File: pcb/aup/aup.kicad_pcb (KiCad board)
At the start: 6 copper layers, 100 x 80 mm, 95 parts, among them IC1 MT41K128M16JT-125_K, IC2 88E1512-A0-NNP2C000, J1 DF40C-100DS-0.4V_51, J2 DF40C-100DS-0.4V_51, J3 DF40C-100DS-0.4V_51, J4 DF40C-100DS-0.4V_51, Q1 AO3401A, Q2 AO3401A, U1 XC7A50T-FGG484, U11 FT2232HQ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

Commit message: First pass on lower rails
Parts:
- F1, Q1: moved to B.Cu
- moved Q1 110.4 mm to (122.5, 54.0), turned to 180 degrees
- moved F1 105.6 mm to (118.0, 56.2), turned to 90 degrees
- moved R24 97.0 mm to (127.1, 124.5), turned to -90 degrees
- moved L5 96.9 mm to (121.4, 121.8), turned to -90 degrees
- moved R25 96.3 mm to (128.7, 124.5), turned to 90 degrees
- moved U7 95.7 mm to (124.5, 120.7)
- moved C25 93.2 mm to (124.5, 118.6)
- moved R26 92.0 mm to (128.7, 121.0), turned to 90 degrees
- moved R27 89.2 mm to (127.1, 121.0), turned to -90 degrees
- moved R32 88.5 mm to (113.7, 124.5), turned to 90 degrees
- moved C32 84.7 mm to (122.7, 125.8)
- moved R33 83.5 mm to (113.7, 121.0), turned to 90 degrees
- moved C29 83.0 mm to (122.7, 124.2)
- moved C21 81.1 mm to (121.3, 116.6), turned to 180 degrees
- moved L7 80.6 mm to (106.4, 121.8), turned to -90 degrees
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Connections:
- net Net-(U4-FB) renamed /power_reg/FB_1V2
- net Net-(U7-FB) renamed /power_reg/FB_1V35
- net Net-(U9-FB) renamed /power_reg/FB_3V3
- R30 pad 2: Net-(U8-FB) -> /power_reg/FB_Vccint
- R31 pad 1: Net-(U8-FB) -> /power_reg/FB_Vccint
- U8 pad 6: Net-(U8-FB) -> /power_reg/FB_Vccint
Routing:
- net +3V3: track 0.00 -> 15.2 mm, vias 0 -> 9
- net +1V35: track 0.00 -> 15.2 mm, vias 0 -> 9
- net GND: track 10.4 -> 15.6 mm, vias 41 -> 61
- net /power_reg/PG_3V3: track 0.00 -> 3.64 mm, vias 0 -> 2
- net /power_reg/PG_1V35: track 0.00 -> 3.64 mm, vias 0 -> 2
- net /power_reg/FB_3V3: track 0.00 -> 3.41 mm
- net /power_reg/FB_1V35: track 0.00 -> 3.41 mm
- net Net-(U8-FB): track 3.41 -> 0.00 mm
- net /power_reg/FB_Vccint: track 3.41 -> 6.82 mm
- net +5V: track 16.3 -> 19.5 mm, vias 17 -> 23
- net /power_reg/SW_3V3: track 0.00 -> 2.30 mm
- net /power_reg/SW_1V35: track 0.00 -> 2.30 mm
- net Net-(R32-Pad2): track 0.00 -> 1.83 mm
- net Net-(R25-Pad2): track 0.00 -> 1.83 mm
- added copper zone on F.Cu, net +1V35
- added copper zone on F.Cu, net +3V3
- added copper zone on In2.Cu, net +5V
- added copper zone on In2.Cu, net +Vccint
- added copper zone on F.Cu, net /power_reg/SW_1V35
- added copper zone on F.Cu, net /power_reg/SW_3V3
- added copper zone on In1.Cu, net GND
- added copper zone on In4.Cu, net GND
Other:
- board text added: "1V35"
- board text added: "3V3"

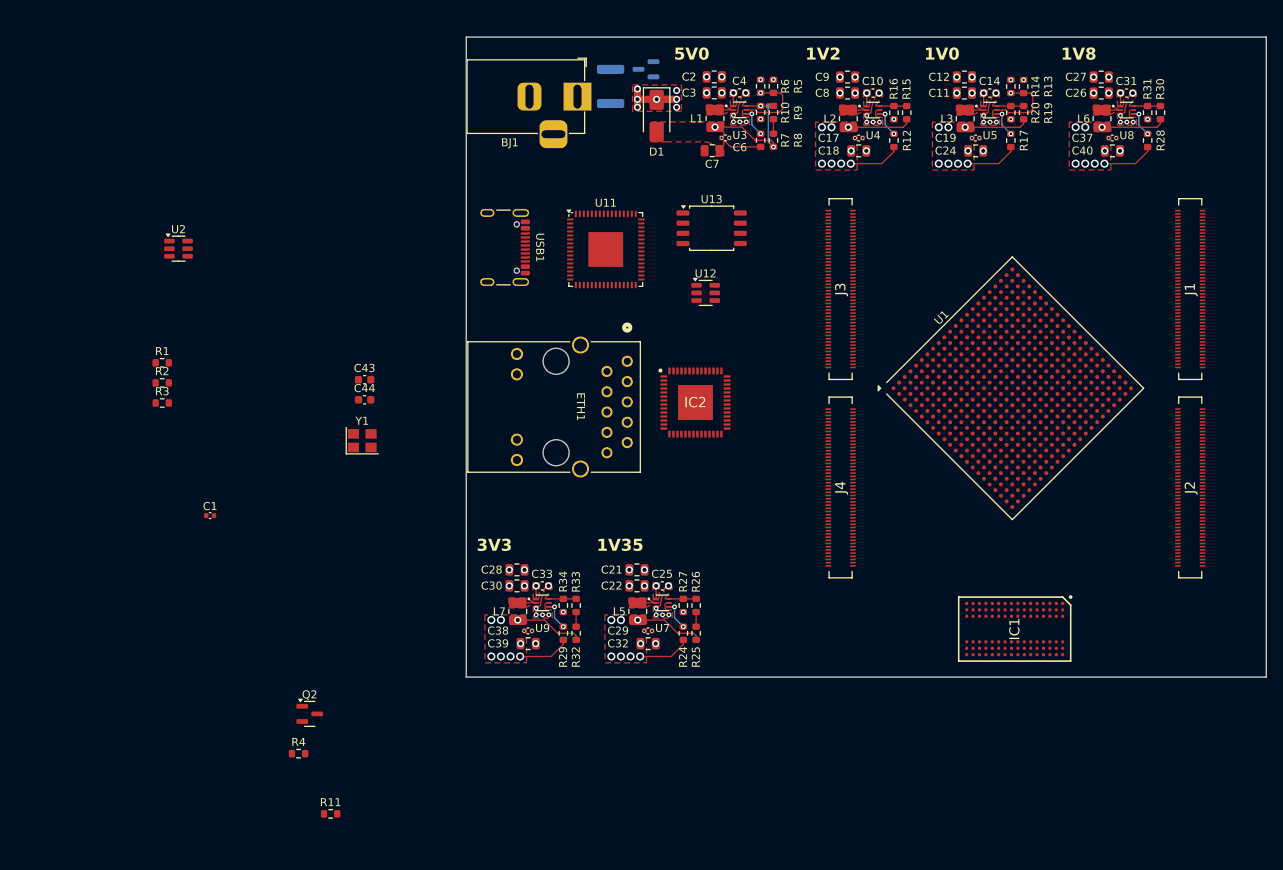
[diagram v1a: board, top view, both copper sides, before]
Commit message: Fix L1 footprint and add reg and ftdi models
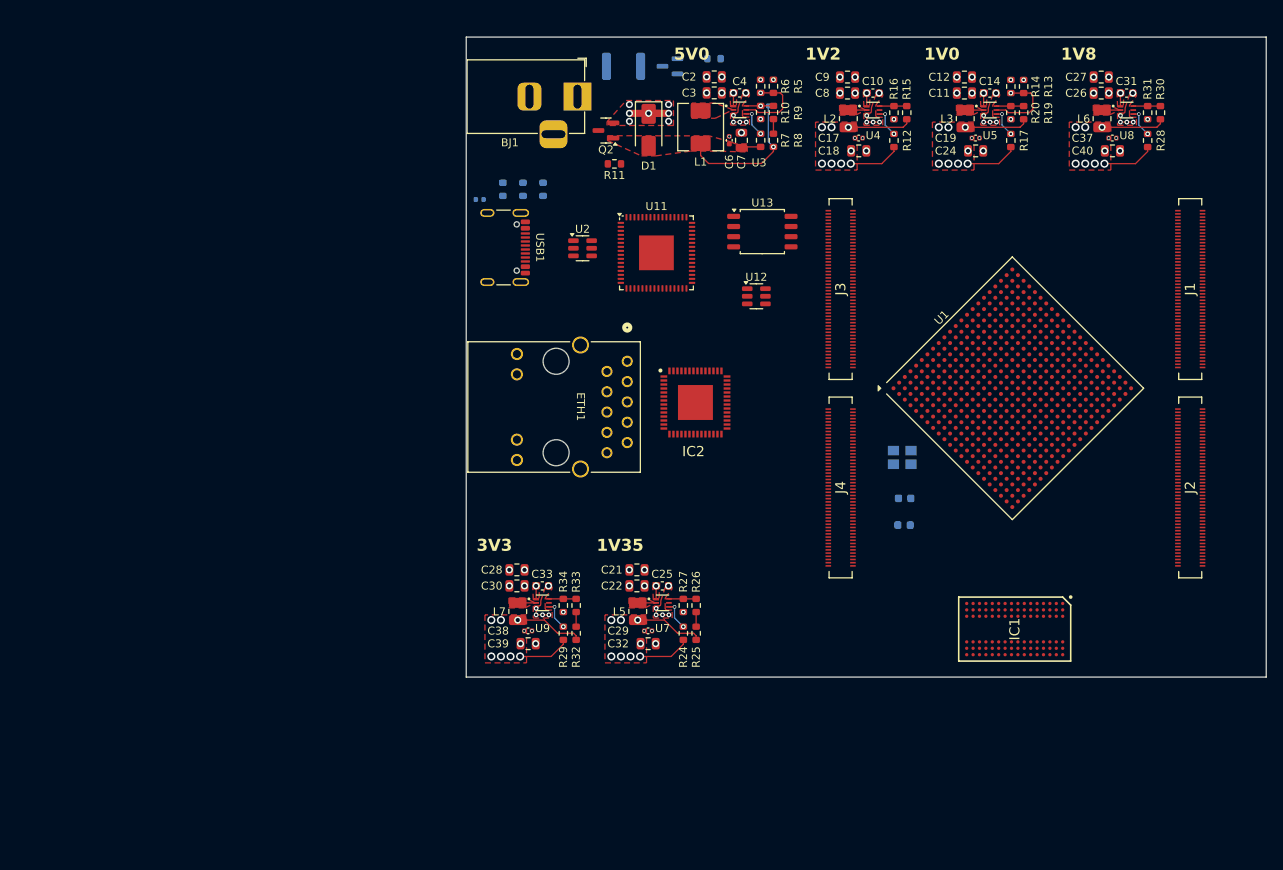
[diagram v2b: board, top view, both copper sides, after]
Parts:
- C1, C43, C44, R1, R2, R3, R4, Y1: moved to B.Cu
- L1: footprint Inductor_SMD:L_1008_2520Metric -> Inductor_SMD:L_Sunlord_MWSA0518S
- U11: footprint Package_DFN_QFN:QFN-64-1EP_9x9mm_P0.5mm_EP4.35x4.35mm -> !Misc:FT2232HQ
- moved R4 101.2 mm to (131.0, 52.7)
- moved R11 88.7 mm to (118.5, 65.8), turned to 180 degrees
- moved Q2 81.8 mm to (117.5, 61.7), turned to 180 degrees
- moved C43 69.8 mm to (154.7, 111.0)
- moved C44 68.6 mm to (154.8, 107.7)
- moved Y1 67.5 mm to (154.5, 102.5)
- moved R3 54.6 mm to (109.6, 69.0), turned to -90 degrees
- moved C1 51.9 mm to (101.7, 70.3)
- moved R2 51.2 mm to (107.1, 69.0), turned to -90 degrees
- moved U2 50.5 mm to (114.5, 76.4)
- moved R1 47.8 mm to (104.6, 69.0), turned to -90 degrees
- moved U11 6.35 mm to (123.8, 77.0)
- moved U12 6.35 mm to (136.3, 82.4)
- moved U13 6.35 mm to (137.0, 74.3)
- moved C7 3.87 mm to (134.4, 62.9), turned to 90 degrees
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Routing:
- net /ext_power/SW_5V4: track 2.30 -> 0.00 mm
- net +5V: track 19.5 -> 17.2 mm
- net /ext_power/REG_5V4: track 19.4 -> 20.2 mm, vias 3 -> 1
- net GND: track 15.6 -> 15.7 mm, vias 61 -> 62

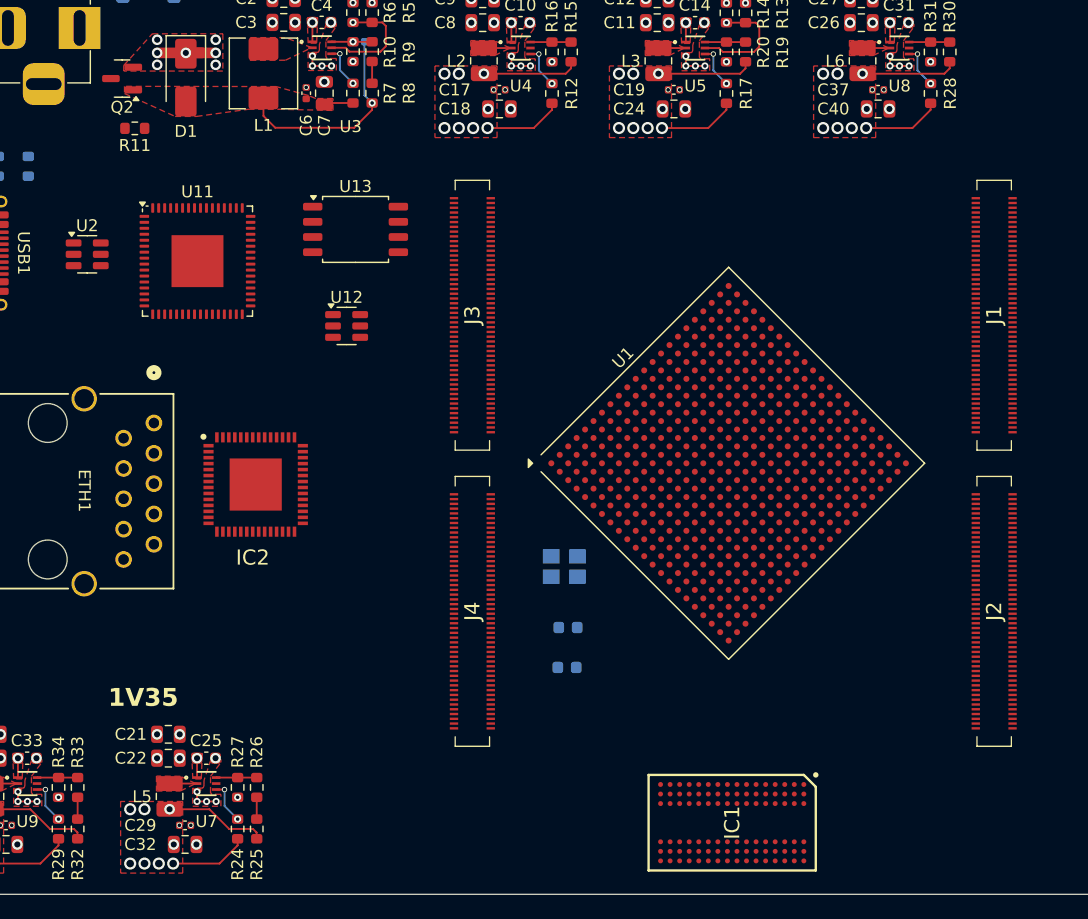
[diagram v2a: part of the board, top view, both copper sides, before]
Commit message: Update footprints and 3d models. All render
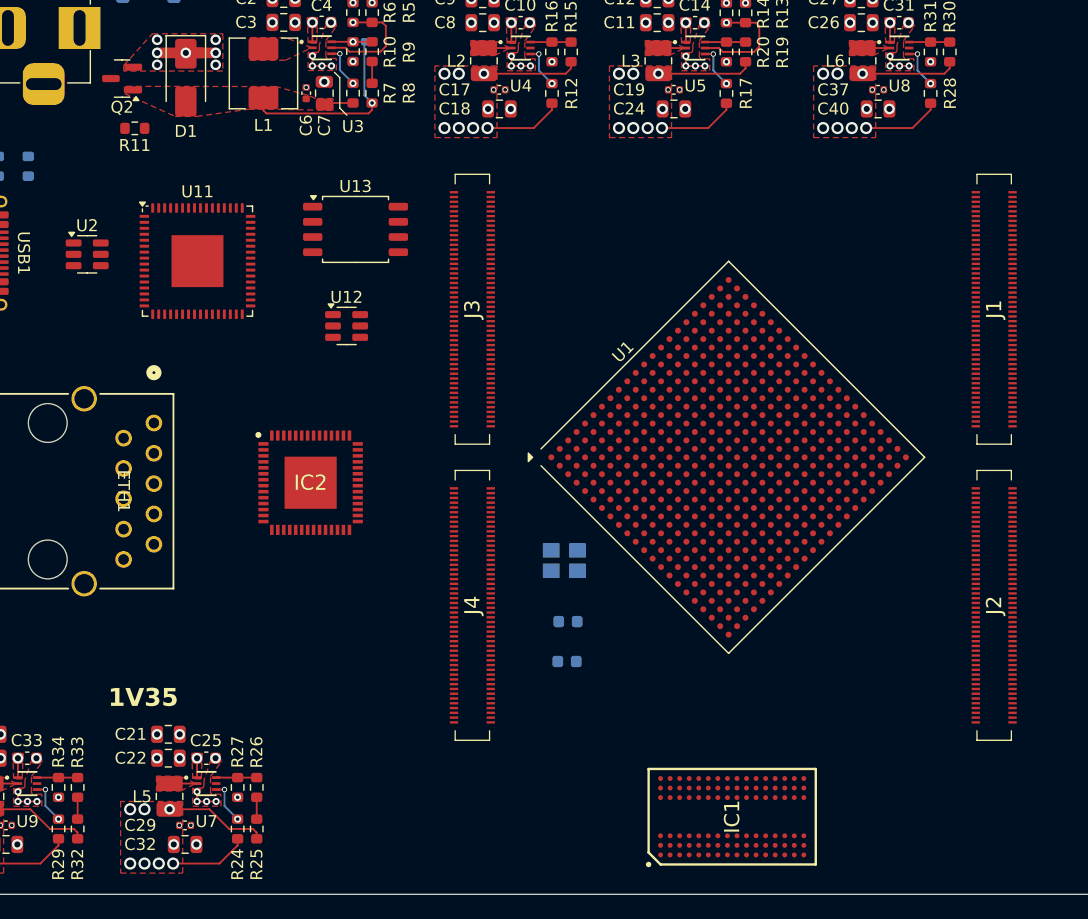
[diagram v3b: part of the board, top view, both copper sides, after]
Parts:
- IC2: footprint !Misc:QFN50P800X800X100-57N-D -> !Misc:88E1512-A0-NNP2C000
- U1: footprint Package_BGA:Xilinx_FGG484 -> !Xilinx:Xilinx_FGG484
- moved IC2 4.60 mm to (133.2, 95.5)
- moved C43 0.50 mm to (154.7, 110.5)
- moved C44 0.50 mm to (154.8, 107.2)
- moved IC1 0.50 mm to (168.6, 123.5), turned to 90 degrees
- moved J1 0.50 mm to (190.5, 81.0)
- moved J2 0.50 mm to (190.5, 105.8)
- moved J3 0.50 mm to (146.8, 81.0)
- moved J4 0.50 mm to (146.8, 105.8)
- moved U1 0.50 mm to (168.3, 93.4)
- moved Y1 0.50 mm to (154.5, 102.0)
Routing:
- net /ext_power/REG_5V4: track 20.2 -> 19.0 mm

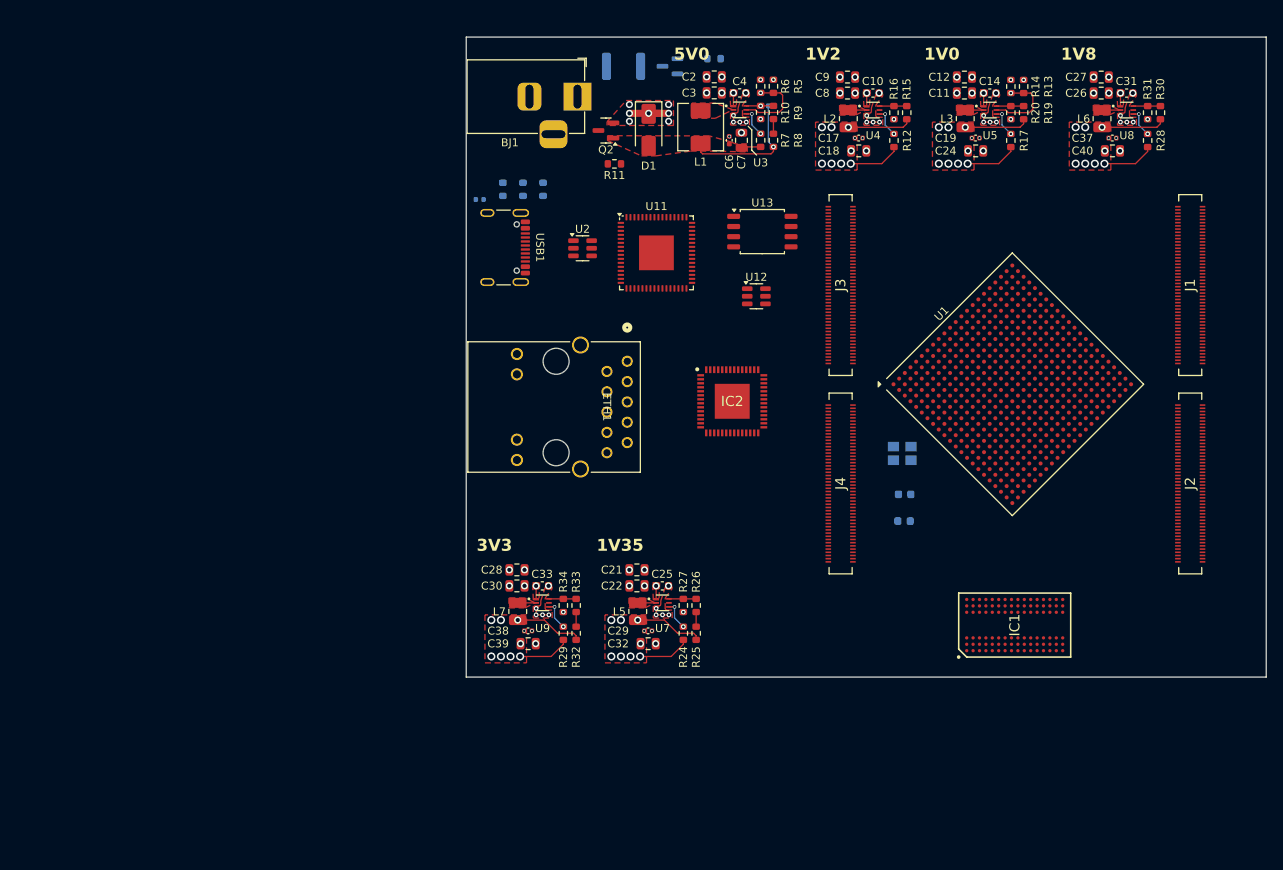
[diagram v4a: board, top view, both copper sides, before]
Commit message: Improve FB nets for lower EMI. Route 5V out to regs
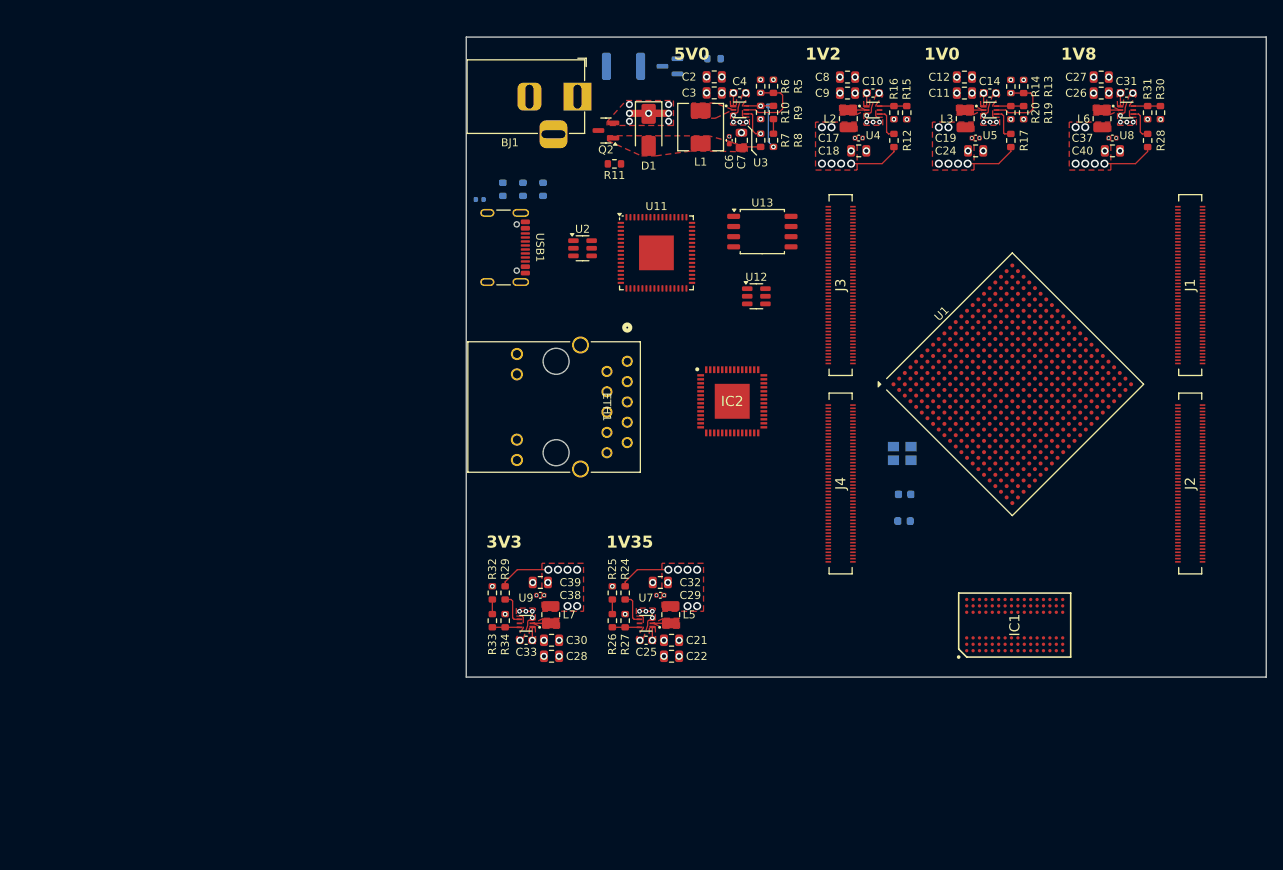
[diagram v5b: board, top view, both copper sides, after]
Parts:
- moved C28 11.6 mm to (110.7, 127.4), turned to 0 degrees
- moved R25 11.6 mm to (118.3, 119.5), turned to -90 degrees
- moved R32 11.6 mm to (103.3, 119.5), turned to -90 degrees
- moved R26 10.6 mm to (118.3, 123.0), turned to -90 degrees
- moved R33 10.6 mm to (103.3, 123.0), turned to -90 degrees
- moved C21 9.81 mm to (125.7, 125.4), turned to 0 degrees
- moved C22 9.81 mm to (125.7, 127.4), turned to 0 degrees
- moved R24 8.86 mm to (119.9, 119.5), turned to 90 degrees
- moved R29 8.86 mm to (104.9, 119.5), turned to 90 degrees
- moved C30 8.06 mm to (110.7, 125.4), turned to 0 degrees
- moved C32 7.80 mm to (124.3, 118.2), turned to 180 degrees
- moved C39 7.80 mm to (109.3, 118.2), turned to 180 degrees
- moved R27 7.52 mm to (119.9, 123.0), turned to 90 degrees
- moved R34 7.52 mm to (104.9, 123.0), turned to 90 degrees
- moved C25 7.09 mm to (122.5, 125.4), turned to 180 degrees
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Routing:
- net /ext_power/REG_5V4: track 19.0 -> 13.7 mm
- net +5V: track 17.2 -> 14.4 mm
- net +3V3: track 15.2 -> 13.5 mm
- net +1V35: track 15.2 -> 13.5 mm
- net /power_reg/PG_Vccint: track 3.64 -> 4.07 mm, vias 2 -> 0
- net /power_reg/PG_3V3: track 3.64 -> 4.05 mm, vias 2 -> 0
- net /power_reg/PG_1V35: track 3.64 -> 4.05 mm, vias 2 -> 0
- net Net-(U3-PG): track 3.64 -> 4.02 mm, vias 2 -> 1
- net /power_reg/PG_1V2: track 3.64 -> 4.01 mm, vias 2 -> 0
- net /power_reg/PG_Vccaux: track 3.64 -> 4.01 mm, vias 2 -> 0
- removed copper zone on In2.Cu, net +Vccint
